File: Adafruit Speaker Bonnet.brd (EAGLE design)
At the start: 65 x 30 mm, 31 parts, among them X1 3.5mm, X2 3.5mm, X3 4 JST-PH

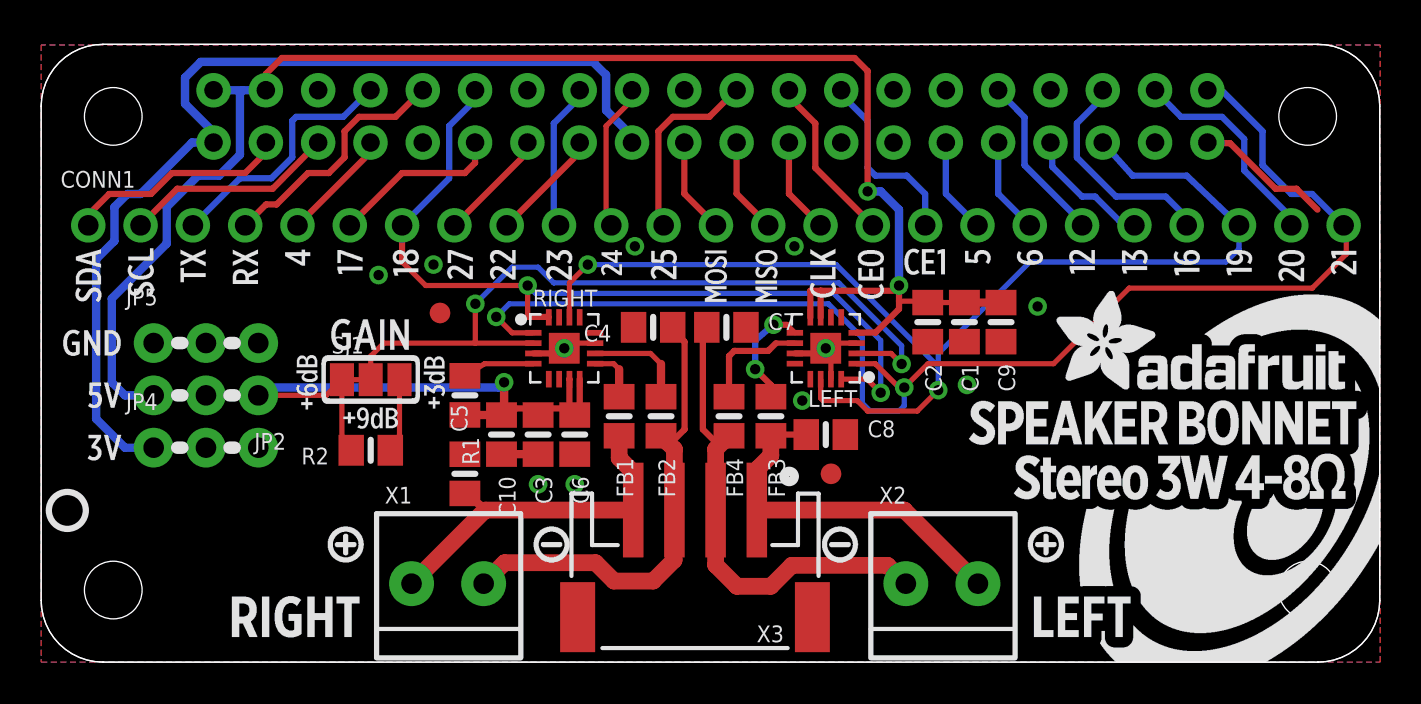
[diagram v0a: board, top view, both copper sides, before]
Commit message: fix pop problem
MAX98357A not in shutdown when no clocks are present (no auto-detect). !SD_MODE is a multi-level comparator with an internal 100k pull-down.
* disconnect !SD_MODE pins from PU to 5V
* connect LEFT channel directly to selector
* connect RIGHT channel through R_SMALL (3.3V:220k) to selector
* selector allows selection between always-on (PU to 3.3V instead of 5V to avoid accidental GPIO bridging to 5V) and GPIO4
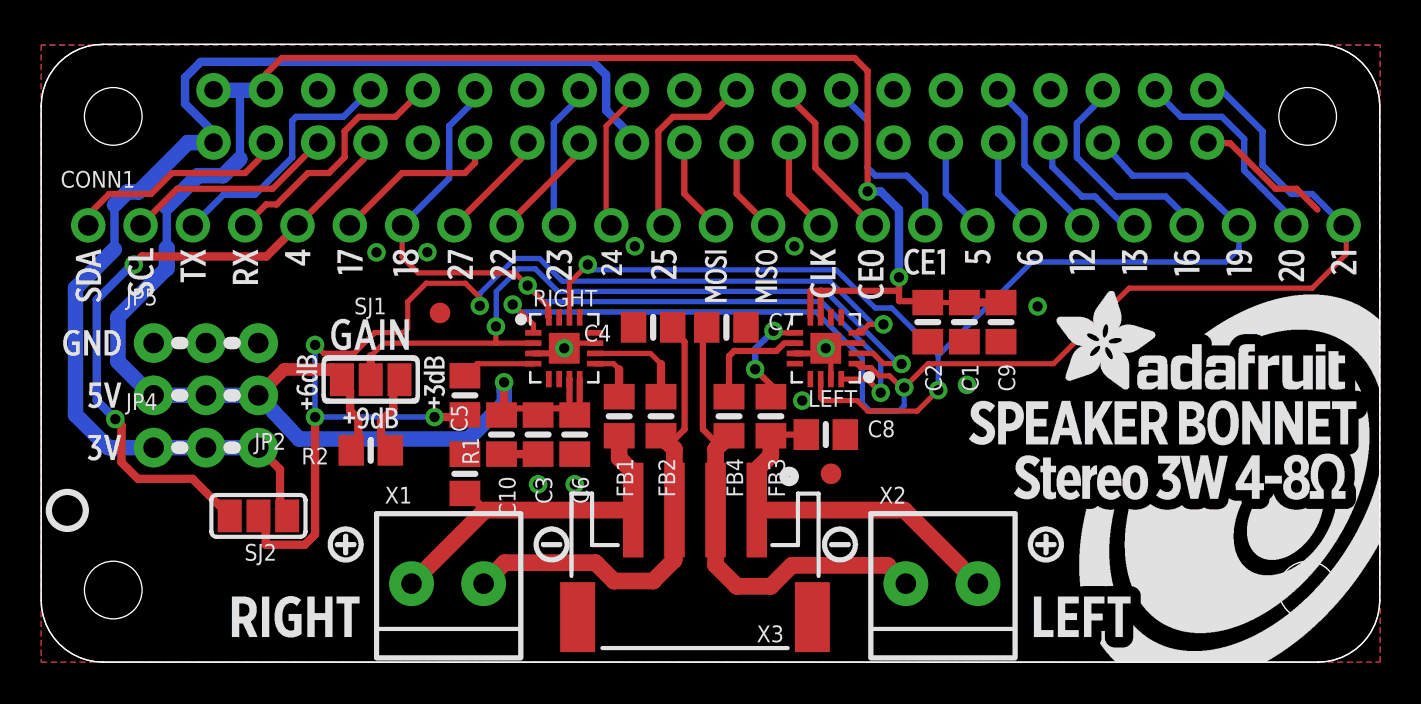
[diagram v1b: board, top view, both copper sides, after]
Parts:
- added SJ2: (no value), microbuilder:SOLDERJUMPER_2WAY_OPEN_NOPASTE
- R1: value 390K -> 220K
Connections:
- new net !SD: LEFT.4, R1.2, SJ2.2
- net 3.3V: now also SJ2.1
- net 5.0V: no longer LEFT.4, R1.2
- net GPIO4: now also SJ2.3
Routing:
- net !SD: track 0.00 -> 55.9 mm, vias 0 -> 5
- net GPIO4: track 5.49 -> 31.4 mm, vias 0 -> 2
- net 3.3V: track 53.8 -> 59.0 mm
- net DIN: track 65.9 -> 63.9 mm
- net 5.0V: track 116.9 -> 115.1 mm
- net BCLK: track 41.9 -> 40.6 mm
- net GAIN: track 37.5 -> 36.3 mm
- net N$4: track 1.14 -> 0.00 mm

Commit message: fix clearance issue arount mounting hole, update readme
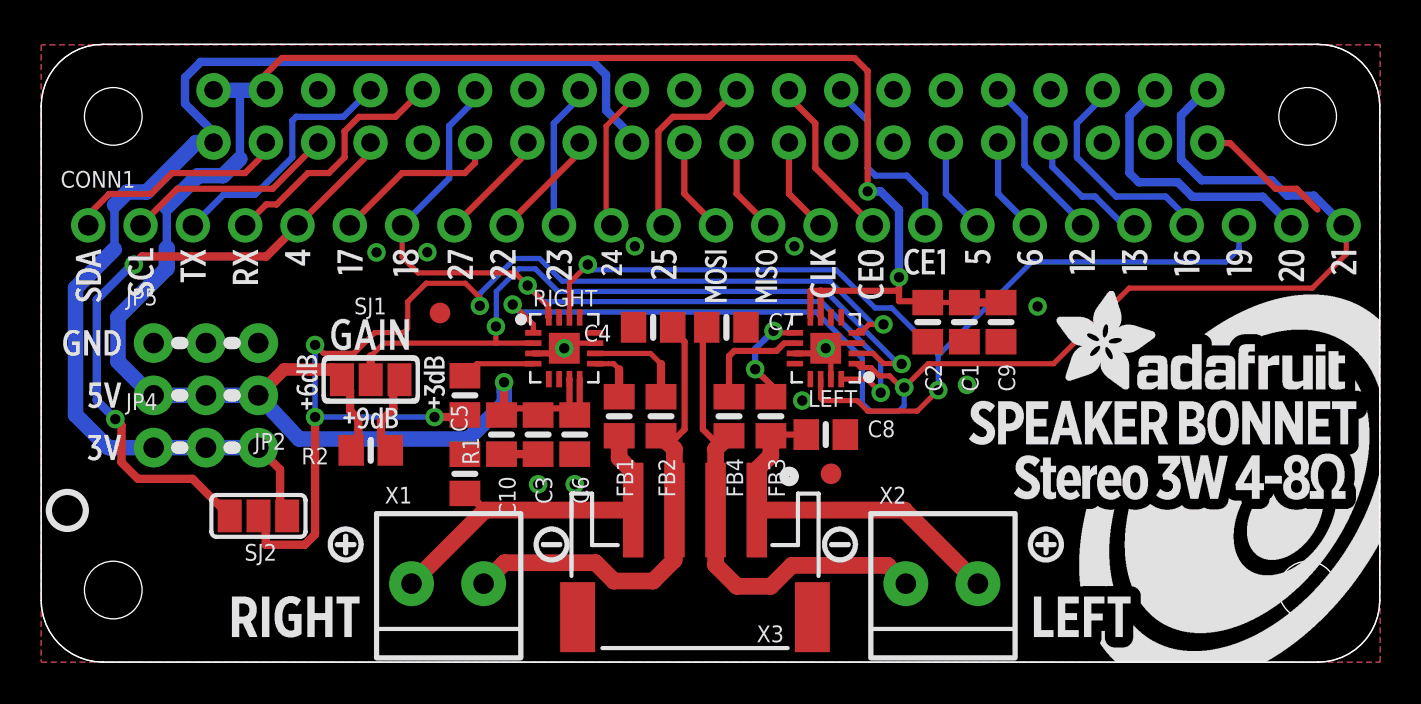
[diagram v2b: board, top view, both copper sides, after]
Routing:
- net LRCLK: track 57.0 -> 48.7 mm
- net GPIO20: track 10.5 -> 13.4 mm
- net DIN: track 63.9 -> 66.8 mm
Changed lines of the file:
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@@
 <setting verticaltext="up"/>
 </settings>
-<grid distance="0.1" unitdist="mm" unit="mm" style="lines" multiple="1" display="no" altdistance="0.025" altunitdist="inch" altunit="inch"/>
+<grid distance="0.05" unitdist="mm" unit="mm" style="lines" multiple="1" display="no" altdistance="0.025" altunitdist="inch" altunit="inch"/>
 <layers>
 <layer number="1" name="Top" color="4" fill="1" visible="yes" active="yes"/>
@@
 <wire x1="5.461" y1="10.414" x2="8.001" y2="10.414" width="0.75" layer="16"/>
 <wire x1="8.001" y1="10.414" x2="10.541" y2="10.414" width="0.75" layer="16"/>
-<wire x1="8.37" y1="25.23" x2="7.123" y2="25.23" width="0.75" layer="16"/>
-<wire x1="7.123" y1="25.23" x2="4.726" y2="22.833" width="0.75" layer="16"/>
-<wire x1="4.726" y1="22.833" x2="4.191" y2="22.833" width="0.75" layer="16"/>
+<wire x1="8.37" y1="25.23" x2="7.523" y2="25.23" width="0.75" layer="16"/>
+<wire x1="7.523" y1="25.23" x2="5.126" y2="22.833" width="0.75" layer="16"/>
+<wire x1="5.126" y1="22.833" x2="4.191" y2="22.833" width="0.75" layer="16"/>
 <wire x1="4.191" y1="22.833" x2="3.556" y2="22.198" width="0.75" layer="16"/>
 <wire x1="3.556" y1="22.198" x2="3.556" y2="20.047" width="0.4064" layer="16"/>
@@
 <contactref element="RPI1" pad="38"/>
 <contactref element="CONN1" pad="24"/>
-<wire x1="54.09" y1="27.77" x2="55.3455" y2="26.4795" width="0.3048" layer="16"/>
-<wire x1="55.3455" y1="26.4795" x2="57.3405" y2="26.4795" width="0.3048" layer="16"/>
-<wire x1="57.3405" y1="26.4795" x2="58.42" y2="25.4" width="0.3048" layer="16"/>
-<wire x1="58.42" y1="25.4" x2="58.42" y2="23.876" width="0.3048" layer="16"/>
-<wire x1="58.42" y1="23.876" x2="60.706" y2="21.59" width="0.3048" layer="16"/>
-<wire x1="60.706" y1="21.59" x2="60.706" y2="21.209" width="0.3048" layer="16"/>
+<wire x1="60.706" y1="21.209" x2="59.315" y2="22.6" width="0.4064" layer="16"/>
+<wire x1="59.315" y1="22.6" x2="55.9" y2="22.6" width="0.4064" layer="16"/>
+<wire x1="55.9" y1="22.6" x2="55.2" y2="23.3" width="0.4064" layer="16"/>
+<wire x1="55.2" y1="23.3" x2="53.3" y2="23.3" width="0.4064" layer="16"/>
+<wire x1="53.3" y1="23.3" x2="52.85" y2="23.75" width="0.4064" layer="16"/>
+<wire x1="52.85" y1="23.75" x2="52.85" y2="26.53" width="0.4064" layer="16"/>
+<wire x1="52.85" y1="26.53" x2="54.09" y2="27.77" width="0.4064" layer="16"/>
 </signal>
 <signal name="GPIO23">
@@
 <contactref element="RPI1" pad="35"/>
 <contactref element="CONN1" pad="23"/>
-<wire x1="51.55" y1="25.23" x2="52.996" y2="23.622" width="0.3048" layer="16"/>
-<wire x1="52.996" y1="23.622" x2="55.626" y2="23.622" width="0.3048" layer="16"/>
-<wire x1="55.626" y1="23.622" x2="58.166" y2="21.209" width="0.3048" layer="16"/>
 <wire x1="37.85" y1="13.74" x2="37.85" y2="12.823" width="0.254" layer="1"/>
 <wire x1="37.85" y1="12.823" x2="37.973" y2="12.7" width="0.254" layer="1"/>
@@
 <wire x1="41.3" y1="17.2" x2="43.561" y2="14.939" width="0.254" layer="16"/>
 <wire x1="43.561" y1="14.939" x2="43.561" y2="14.886" width="0.254" layer="16"/>
+<wire x1="48.106" y1="19.431" x2="51.55" y2="25.23" width="0" layer="19" extent="16-16"/>
 </signal>
 <signal name="DIN">
@@
 <contactref element="RPI1" pad="40"/>
 <contactref element="CONN1" pad="25"/>
-<wire x1="61.722" y1="22.733" x2="63.246" y2="21.209" width="0.3048" layer="16"/>
-<wire x1="61.722" y1="22.733" x2="60.706" y2="22.733" width="0.3048" layer="16"/>
-<wire x1="60.706" y1="22.733" x2="59.309" y2="24.13" width="0.3048" layer="16"/>
-<wire x1="59.309" y1="24.13" x2="59.309" y2="25.781" width="0.3048" layer="16"/>
-<wire x1="59.309" y1="25.781" x2="57.404" y2="27.686" width="0.3048" layer="16"/>
-<wire x1="57.404" y1="27.686" x2="56.679" y2="27.686" width="0.3048" layer="16"/>
 <wire x1="49.161" y1="14.49" x2="52.832" y2="18.161" width="0.254" layer="1"/>
 <wire x1="52.832" y1="18.161" x2="61.722" y2="18.161" width="0.254" layer="1"/>
@@
 <wire x1="49.161" y1="14.49" x2="43.065" y2="14.49" width="0.254" layer="1"/>
 <wire x1="43.065" y1="14.49" x2="41.91" y2="13.335" width="0.254" layer="1"/>
-<wire x1="56.679" y1="27.686" x2="56.63" y2="27.735" width="0.254" layer="16"/>
-<wire x1="56.63" y1="27.735" x2="56.63" y2="27.77" width="0.254" layer="16"/>
 <wire x1="23.9" y1="15.99" x2="23.9" y2="16.4" width="0.254" layer="1"/>
 <wire x1="23.9" y1="16.4" x2="22.936" y2="17.364" width="0.254" layer="1"/>
@@
 <wire x1="41.2" y1="13.9" x2="41.765" y2="13.335" width="0.254" layer="1"/>
 <wire x1="41.765" y1="13.335" x2="41.91" y2="13.335" width="0.254" layer="1"/>
+<wire x1="63.246" y1="21.209" x2="61.805" y2="22.65" width="0.4064" layer="16"/>
+<wire x1="61.805" y1="22.65" x2="60.5" y2="22.65" width="0.4064" layer="16"/>
+<wire x1="60.5" y1="22.65" x2="59.75" y2="23.4" width="0.4064" layer="16"/>
+<wire x1="59.75" y1="23.4" x2="56.35" y2="23.4" width="0.4064" layer="16"/>
+<wire x1="56.35" y1="23.4" x2="55.35" y2="24.4" width="0.4064" layer="16"/>
+<wire x1="55.35" y1="24.4" x2="55.35" y2="26.55" width="0.4064" layer="16"/>
+<wire x1="55.35" y1="26.55" x2="56.57" y2="27.77" width="0.4064" layer="16"/>
+<wire x1="56.57" y1="27.77" x2="56.63" y2="27.77" width="0.4064" layer="16"/>
 </signal>
 <signal name="GAIN">

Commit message: reconnect missing signal
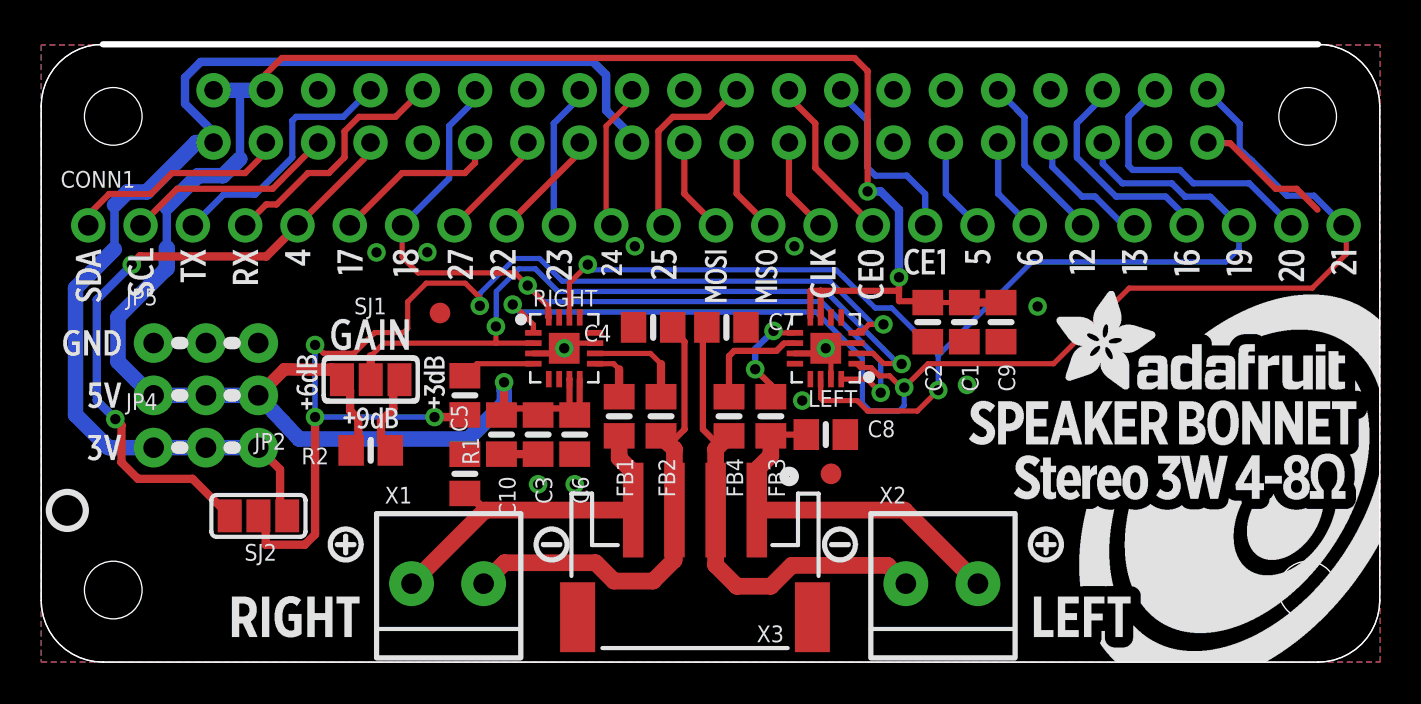
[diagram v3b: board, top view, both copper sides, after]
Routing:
- net LRCLK: track 48.7 -> 57.6 mm
- net DIN: track 66.8 -> 63.8 mm
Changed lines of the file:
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@@
 <wire x1="65" y1="3" x2="65" y2="27" width="0" layer="20"/>
 <wire x1="65" y1="27" x2="62" y2="30" width="0" layer="20" curve="90"/>
-<wire x1="62" y1="30" x2="3" y2="30" width="0" layer="20"/>
+<wire x1="62" y1="30" x2="3" y2="30" width="0.3048" layer="20"/>
 <wire x1="3" y1="30" x2="0" y2="27" width="0" layer="20" curve="90"/>
 <wire x1="0" y1="27" x2="0" y2="3" width="0" layer="20"/>
@@
 <contactref element="SJ2" pad="3"/>
 <wire x1="12.446" y1="21.209" x2="10.937" y2="19.7" width="0.4096" layer="1"/>
-<wire x1="10.937" y1="19.7" x2="4.9" y2="19.7" width="0.4096" layer="1"/>
-<wire x1="4.9" y1="19.7" x2="4.5" y2="19.3" width="0.4096" layer="1"/>
-<via x="4.5" y="19.3" extent="1-16" drill="0.5"/>
+<wire x1="10.937" y1="19.7" x2="4.8" y2="19.7" width="0.4096" layer="1"/>
+<wire x1="4.8" y1="19.7" x2="4.4" y2="19.3" width="0.4096" layer="1"/>
+<via x="4.4" y="19.3" extent="1-16" drill="0.5"/>
 <wire x1="4.4" y1="19.3" x2="2.7" y2="17.6" width="0.4064" layer="16"/>
 <wire x1="2.7" y1="17.6" x2="2.7" y2="12.7" width="0.4064" layer="16"/>
@@
 <wire x1="4.7" y1="8.9" x2="7.353" y2="8.9" width="0.4064" layer="1"/>
 <wire x1="7.353" y1="8.9" x2="9.153" y2="7.1" width="0.4064" layer="1"/>
-<wire x1="4.4" y1="19.3" x2="4.5" y2="19.3" width="0" layer="19" extent="1-16"/>
 </signal>
 <signal name="GPIO17">
@@
 <contactref element="RPI1" pad="38"/>
 <contactref element="CONN1" pad="24"/>
-<wire x1="60.706" y1="21.209" x2="59.315" y2="22.6" width="0.4064" layer="16"/>
-<wire x1="59.315" y1="22.6" x2="55.9" y2="22.6" width="0.4064" layer="16"/>
-<wire x1="55.9" y1="22.6" x2="55.2" y2="23.3" width="0.4064" layer="16"/>
-<wire x1="55.2" y1="23.3" x2="53.3" y2="23.3" width="0.4064" layer="16"/>
-<wire x1="53.3" y1="23.3" x2="52.85" y2="23.75" width="0.4064" layer="16"/>
-<wire x1="52.85" y1="23.75" x2="52.85" y2="26.53" width="0.4064" layer="16"/>
-<wire x1="52.85" y1="26.53" x2="54.09" y2="27.77" width="0.4064" layer="16"/>
+<wire x1="60.706" y1="21.209" x2="58.665" y2="23.25" width="0.3048" layer="16"/>
+<wire x1="54.09" y1="27.77" x2="52.8" y2="26.48" width="0.3048" layer="16"/>
+<wire x1="52.8" y1="26.48" x2="52.8" y2="24.1" width="0.3048" layer="16"/>
+<wire x1="52.8" y1="24.1" x2="53" y2="23.9" width="0.3048" layer="16"/>
+<wire x1="53" y1="23.9" x2="55.3" y2="23.9" width="0.3048" layer="16"/>
+<wire x1="55.3" y1="23.9" x2="55.95" y2="23.25" width="0.3048" layer="16"/>
+<wire x1="55.95" y1="23.25" x2="58.665" y2="23.25" width="0.3048" layer="16"/>
 </signal>
 <signal name="GPIO23">
@@
 <wire x1="41.3" y1="17.2" x2="43.561" y2="14.939" width="0.254" layer="16"/>
 <wire x1="43.561" y1="14.939" x2="43.561" y2="14.886" width="0.254" layer="16"/>
-<wire x1="48.106" y1="19.431" x2="51.55" y2="25.23" width="0" layer="19" extent="16-16"/>
+<wire x1="51.55" y1="25.23" x2="51.55" y2="24.2" width="0.3048" layer="16"/>
+<wire x1="51.55" y1="24.2" x2="52.5" y2="23.25" width="0.3048" layer="16"/>
+<wire x1="52.5" y1="23.25" x2="54.9" y2="23.25" width="0.3048" layer="16"/>
+<wire x1="54.9" y1="23.25" x2="55.55" y2="22.6" width="0.3048" layer="16"/>
+<wire x1="55.55" y1="22.6" x2="56.775" y2="22.6" width="0.3048" layer="16"/>
+<wire x1="56.775" y1="22.6" x2="58.166" y2="21.209" width="0.3048" layer="16"/>
 </signal>
 <signal name="DIN">
@@
 <wire x1="41.2" y1="13.9" x2="41.765" y2="13.335" width="0.254" layer="1"/>
 <wire x1="41.765" y1="13.335" x2="41.91" y2="13.335" width="0.254" layer="1"/>
-<wire x1="63.246" y1="21.209" x2="61.805" y2="22.65" width="0.4064" layer="16"/>
-<wire x1="61.805" y1="22.65" x2="60.5" y2="22.65" width="0.4064" layer="16"/>
-<wire x1="60.5" y1="22.65" x2="59.75" y2="23.4" width="0.4064" layer="16"/>
-<wire x1="59.75" y1="23.4" x2="56.35" y2="23.4" width="0.4064" layer="16"/>
-<wire x1="56.35" y1="23.4" x2="55.35" y2="24.4" width="0.4064" layer="16"/>
-<wire x1="55.35" y1="24.4" x2="55.35" y2="26.55" width="0.4064" layer="16"/>
-<wire x1="55.35" y1="26.55" x2="56.57" y2="27.77" width="0.4064" layer="16"/>
+<wire x1="63.246" y1="21.209" x2="61.805" y2="22.65" width="0.3048" layer="16"/>
+<wire x1="61.805" y1="22.65" x2="60.5" y2="22.65" width="0.3048" layer="16"/>
 <wire x1="56.57" y1="27.77" x2="56.63" y2="27.77" width="0.4064" layer="16"/>
+<wire x1="56.57" y1="27.77" x2="58.2" y2="26.14" width="0.3048" layer="16"/>
+<wire x1="58.2" y1="26.14" x2="58.2" y2="24.9" width="0.3048" layer="16"/>
+<wire x1="58.2" y1="24.9" x2="58.8" y2="24.35" width="0.3048" layer="16"/>
+<wire x1="58.8" y1="24.35" x2="60.5" y2="22.65" width="0.3048" layer="16"/>
 </signal>
 <signal name="GAIN">
